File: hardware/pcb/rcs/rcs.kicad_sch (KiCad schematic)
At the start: 19 parts, among them J1 Conn_01x02_Socket, J2 Conn_01x02_Socket, J3 Conn_01x02_Socket, J4 Conn_01x02_Socket, J5 Conn_01x02_Socket, J6 Conn_01x02_Socket, Q1 BS170, Q2 BS170, Q3 BS170, Q4 BS170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

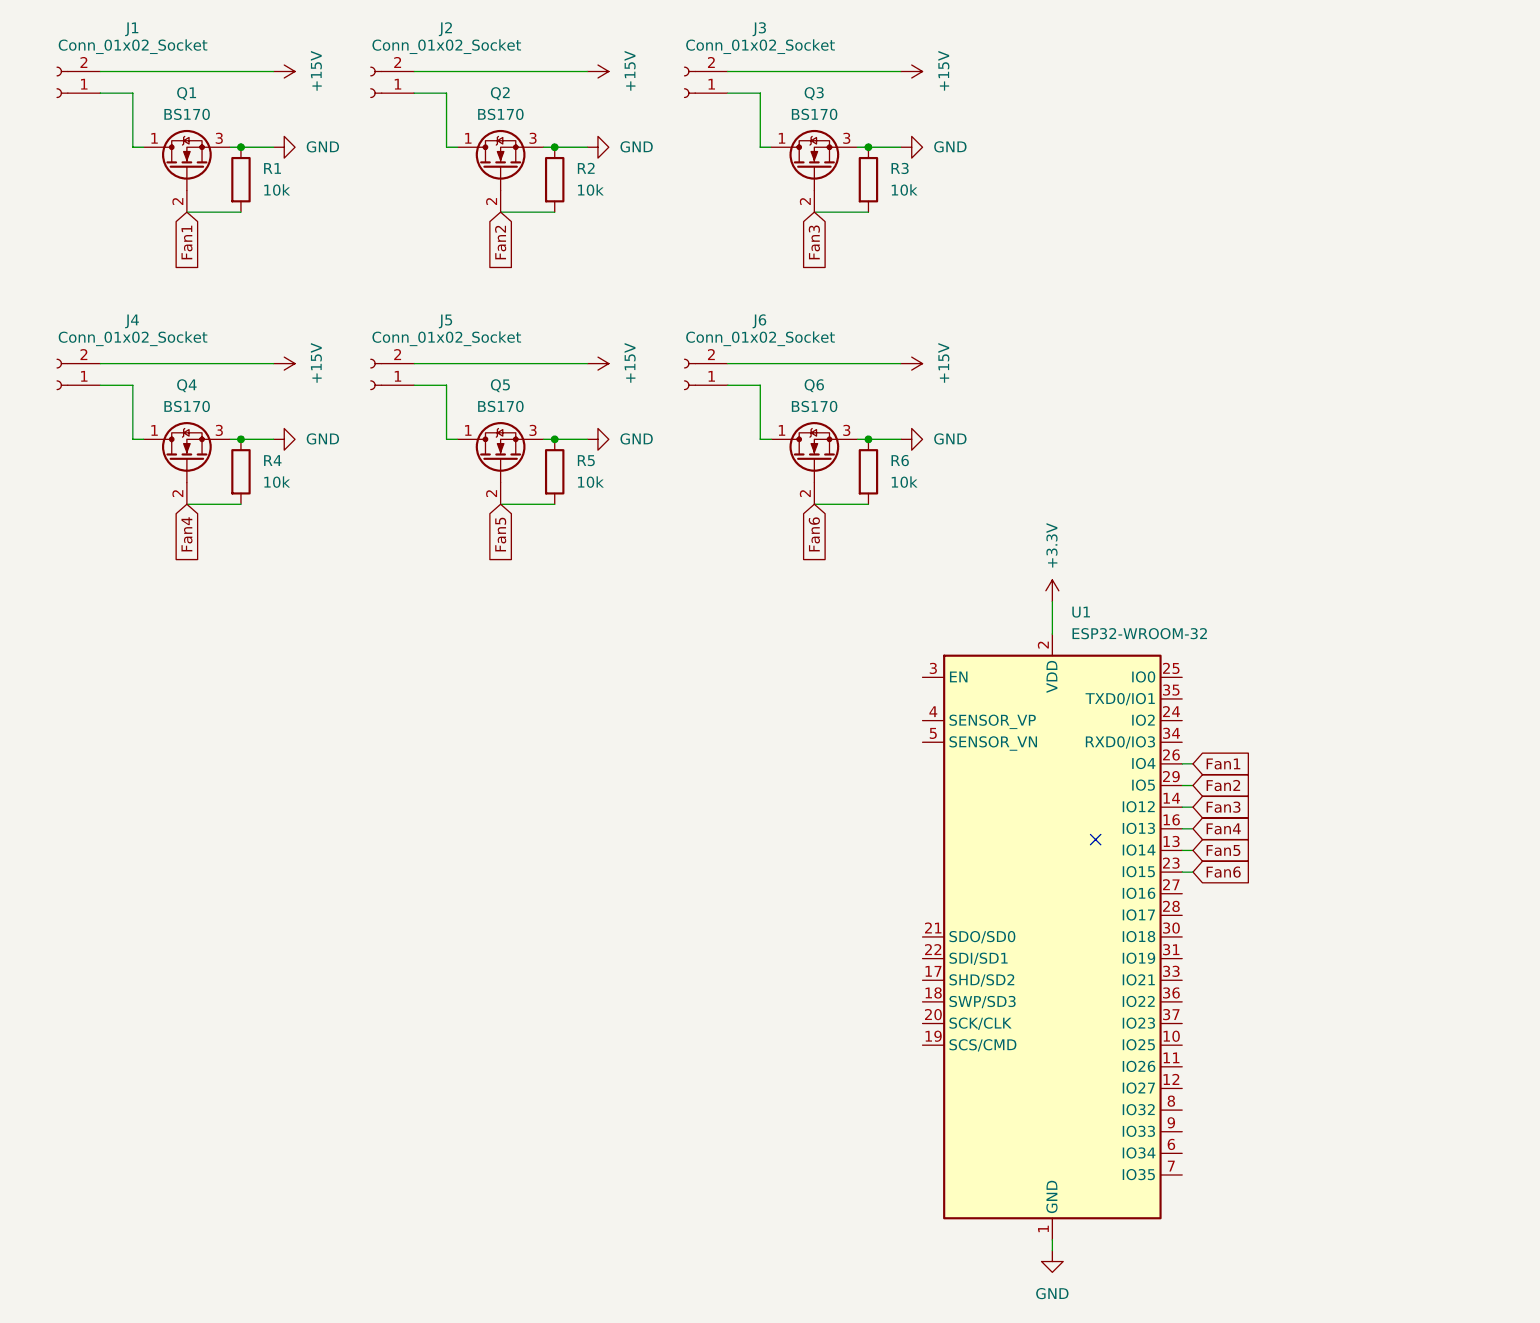
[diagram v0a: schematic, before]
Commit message: Add ESP32 dev board schematic and footprint, make draft PCB
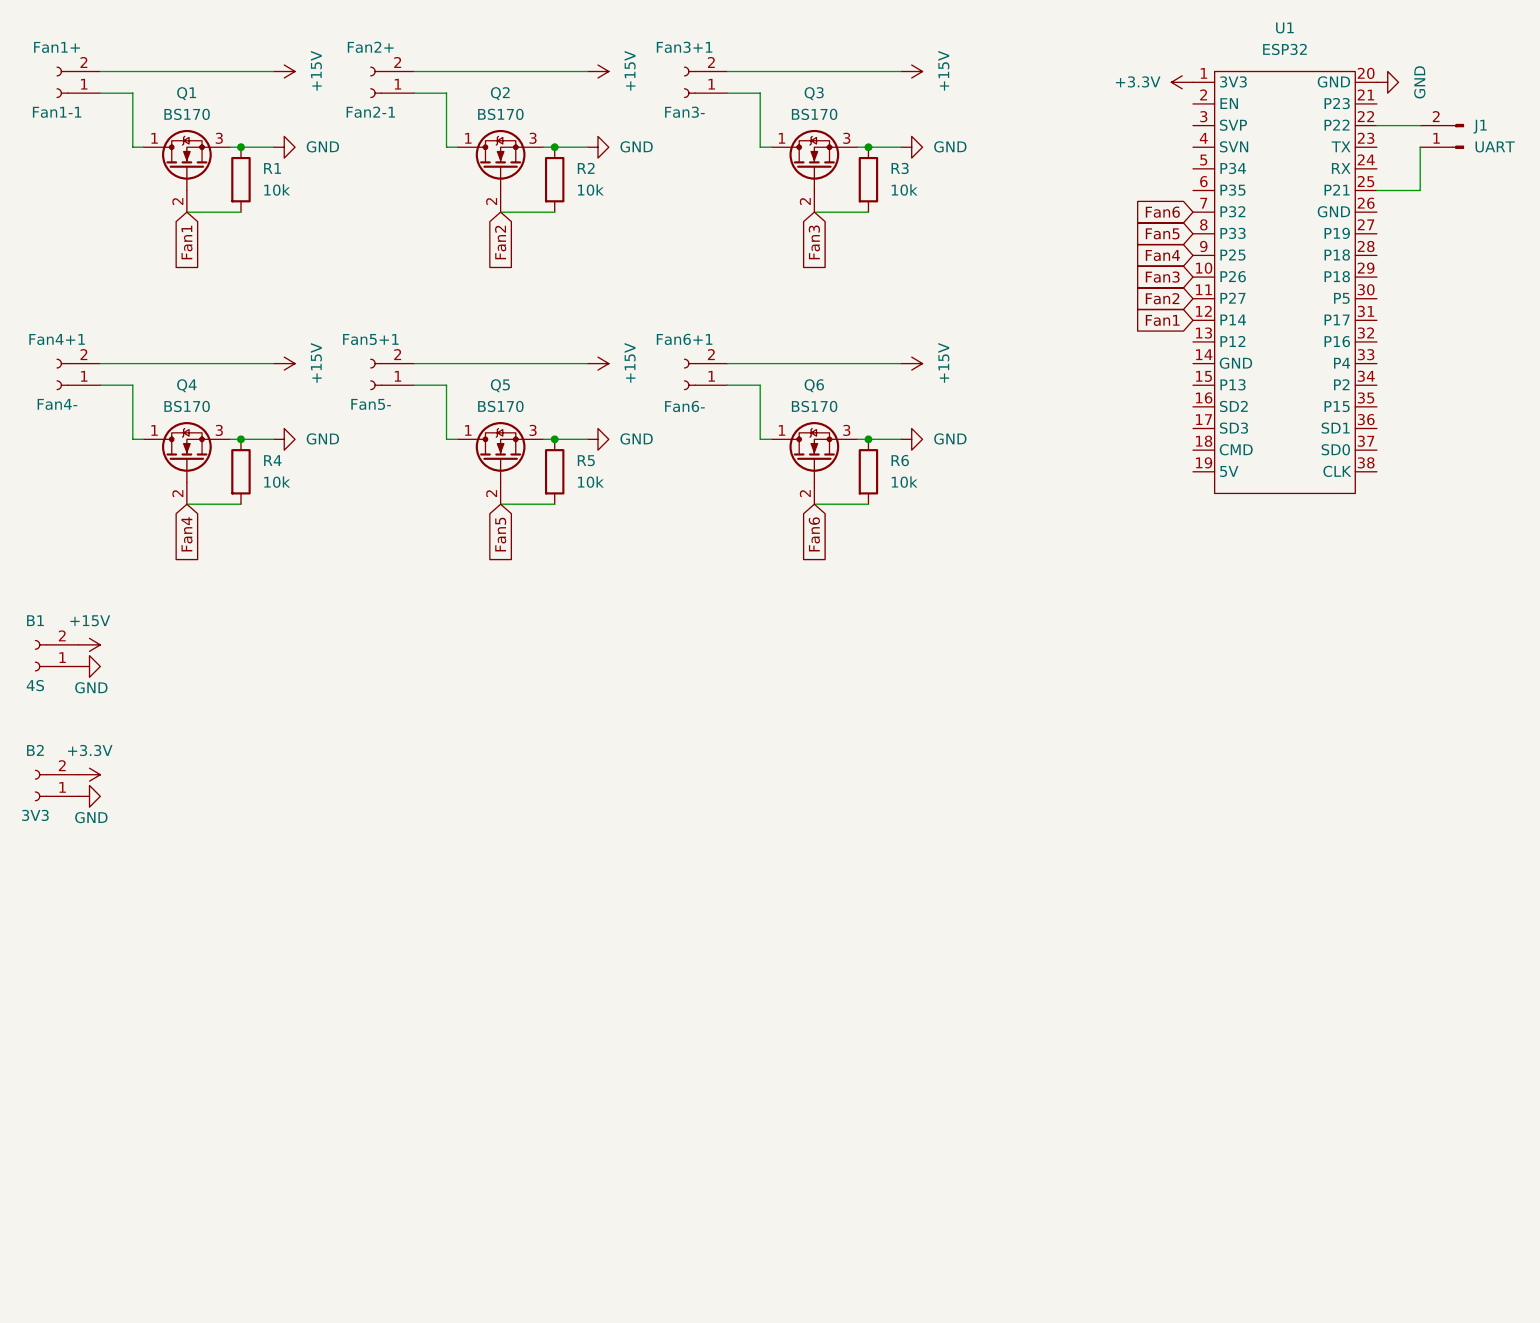
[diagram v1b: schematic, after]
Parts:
- removed U1: ESP32-WROOM-32, RF_Module:ESP32-WROOM-32, symbol RF_Module:ESP32-WROOM-32
- added B1: 4S, Connector_PinHeader_2.54mm:PinHeader_2x02_P2.54mm_Vertical, symbol Connector:Conn_01x02_Socket
- added B2: 3V3, Connector_PinHeader_2.54mm:PinHeader_2x02_P2.54mm_Vertical, symbol Connector:Conn_01x02_Socket
- added J1: UART, Connector_PinHeader_2.54mm:PinHeader_2x02_P2.54mm_Vertical, symbol Connector:Conn_01x02_Pin
- added U1: ESP32, custom:ESP32, symbol custom:ESP32
- Fan1-1: renamed from J1; value Conn_01x02_Socket -> Fan1+
- Fan2-1: renamed from J2; value Conn_01x02_Socket -> Fan2+
- Fan3+1: renamed from J3; value Conn_01x02_Socket -> Fan3-
- Fan4+1: renamed from J4; value Conn_01x02_Socket -> Fan4-
- Fan5+1: renamed from J5; value Conn_01x02_Socket -> Fan5-
- Fan6+1: renamed from J6; value Conn_01x02_Socket -> Fan6-
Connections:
- net +15V: now also B1.2 (Pin_2)
- net +3.3V: now also B2.2 (Pin_2), U1.1 (3V3)
- net Fan1: now also U1.12 (P14)
- net Fan2: now also U1.11 (P27)
- net Fan3: now also U1.10 (P26)
- net Fan4: now also U1.9 (P25)
- net Fan5: now also U1.8 (P33)
- net Fan6: now also U1.7 (P32)
- net GND: now also B1.1 (Pin_1), B2.1 (Pin_1), U1.20 (GND)
- new net: J1.1 (Pin_1), U1.25 (P21)
- new net: J1.2 (Pin_2), U1.22 (P22)
- no-connect marks 1 -> 0

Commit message: More compact PCB layout
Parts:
- B1, B2, J1: footprint Connector_PinHeader_2.54mm:PinHeader_2x02_P2.54mm_Vertical -> Connector_PinHeader_2.54mm:PinHeader_1x02_P2.54mm_Vertical
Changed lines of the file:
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@@
 			)
 		)
-		(property "Footprint" "Connector_PinHeader_2.54mm:PinHeader_2x02_P2.54mm_Vertical"
+		(property "Footprint" "Connector_PinHeader_2.54mm:PinHeader_1x02_P2.54mm_Vertical"
 			(at 191.77 34.29 0)
 			(effects
@@
 			)
 		)
-		(property "Footprint" "Connector_PinHeader_2.54mm:PinHeader_2x02_P2.54mm_Vertical"
+		(property "Footprint" "Connector_PinHeader_2.54mm:PinHeader_1x02_P2.54mm_Vertical"
 			(at 24.13 110.49 0)
 			(effects
@@
 			)
 		)
-		(property "Footprint" "Connector_PinHeader_2.54mm:PinHeader_2x02_P2.54mm_Vertical"
+		(property "Footprint" "Connector_PinHeader_2.54mm:PinHeader_1x02_P2.54mm_Vertical"
 			(at 24.13 95.25 0)
 			(effects

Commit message: Add minimum trace width and screw holes
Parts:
- Fan1-1, Fan2-1, Fan3+1, Fan4+1, Fan5+1, Fan6+1: footprint Connector_Wire:SolderWire-0.25sqmm_1x02_P4.2mm_D0.65mm_OD1.7mm -> Connector_PinHeader_2.54mm:PinHeader_1x02_P2.54mm_Vertical
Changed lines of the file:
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@@
 (kicad_sch
-	(version 20231120)
+	(version 20250114)
 	(generator "eeschema")
-	(generator_version "8.0")
+	(generator_version "9.0")
 	(paper "A4")
 	(junction
@@
 			)
 		)
-		(property "Footprint" "Connector_Wire:SolderWire-0.25sqmm_1x02_P4.2mm_D0.65mm_OD1.7mm"
+		(property "Footprint" "Connector_PinHeader_2.54mm:PinHeader_1x02_P2.54mm_Vertical"
 			(at 100.33 62.23 0)
 			(effects
@@
 			)
 		)
-		(property "Footprint" "Connector_Wire:SolderWire-0.25sqmm_1x02_P4.2mm_D0.65mm_OD1.7mm"
+		(property "Footprint" "Connector_PinHeader_2.54mm:PinHeader_1x02_P2.54mm_Vertical"
 			(at 100.33 27.94 0)
 			(effects
@@
 			)
 		)
-		(property "Footprint" "Connector_Wire:SolderWire-0.25sqmm_1x02_P4.2mm_D0.65mm_OD1.7mm"
+		(property "Footprint" "Connector_PinHeader_2.54mm:PinHeader_1x02_P2.54mm_Vertical"
 			(at 63.5 27.94 0)
 			(effects
@@
 			)
 		)
-		(property "Footprint" "Connector_Wire:SolderWire-0.25sqmm_1x02_P4.2mm_D0.65mm_OD1.7mm"
+		(property "Footprint" "Connector_PinHeader_2.54mm:PinHeader_1x02_P2.54mm_Vertical"
 			(at 63.5 62.23 0)
 			(effects
@@
 			)
 		)
-		(property "Footprint" "Connector_Wire:SolderWire-0.25sqmm_1x02_P4.2mm_D0.65mm_OD1.7mm"
+		(property "Footprint" "Connector_PinHeader_2.54mm:PinHeader_1x02_P2.54mm_Vertical"
 			(at 26.67 27.94 0)
 			(effects
@@
 			)
 		)
-		(property "Footprint" "Connector_Wire:SolderWire-0.25sqmm_1x02_P4.2mm_D0.65mm_OD1.7mm"
+		(property "Footprint" "Connector_PinHeader_2.54mm:PinHeader_1x02_P2.54mm_Vertical"
 			(at 26.67 62.23 0)
 			(effects
@@
 		)
 	)
+	(embedded_fonts no)
 )

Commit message: Increase trace width to 0.3mm
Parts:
- Q1, Q2, Q3, Q4, Q5, Q6: footprint Package_TO_SOT_THT:TO-92_Inline -> Package_TO_SOT_THT:TO-92_Inline_Wide
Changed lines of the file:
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@@
 			)
 		)
-		(property "Footprint" "Package_TO_SOT_THT:TO-92_Inline"
+		(property "Footprint" "Package_TO_SOT_THT:TO-92_Inline_Wide"
 			(at 80.645 31.75 0)
 			(effects
@@
 			)
 		)
-		(property "Footprint" "Package_TO_SOT_THT:TO-92_Inline"
+		(property "Footprint" "Package_TO_SOT_THT:TO-92_Inline_Wide"
 			(at 80.645 66.04 0)
 			(effects
@@
 			)
 		)
-		(property "Footprint" "Package_TO_SOT_THT:TO-92_Inline"
+		(property "Footprint" "Package_TO_SOT_THT:TO-92_Inline_Wide"
 			(at 43.815 31.75 0)
 			(effects
@@
 			)
 		)
-		(property "Footprint" "Package_TO_SOT_THT:TO-92_Inline"
+		(property "Footprint" "Package_TO_SOT_THT:TO-92_Inline_Wide"
 			(at 43.815 66.04 0)
 			(effects
@@
 			)
 		)
-		(property "Footprint" "Package_TO_SOT_THT:TO-92_Inline"
+		(property "Footprint" "Package_TO_SOT_THT:TO-92_Inline_Wide"
 			(at 117.475 31.75 0)
 			(effects
@@
 			)
 		)
-		(property "Footprint" "Package_TO_SOT_THT:TO-92_Inline"
+		(property "Footprint" "Package_TO_SOT_THT:TO-92_Inline_Wide"
 			(at 117.475 66.04 0)
 			(effects

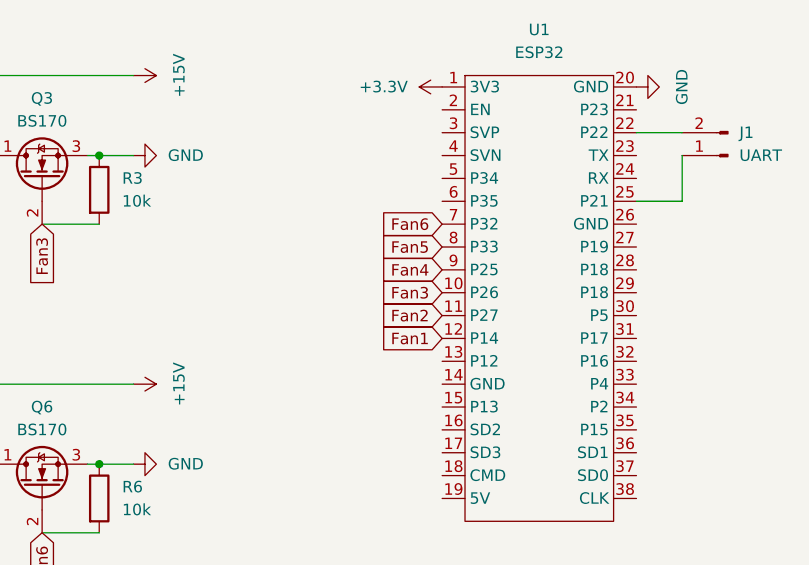
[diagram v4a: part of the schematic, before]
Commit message: Fix ESP32 USB port location
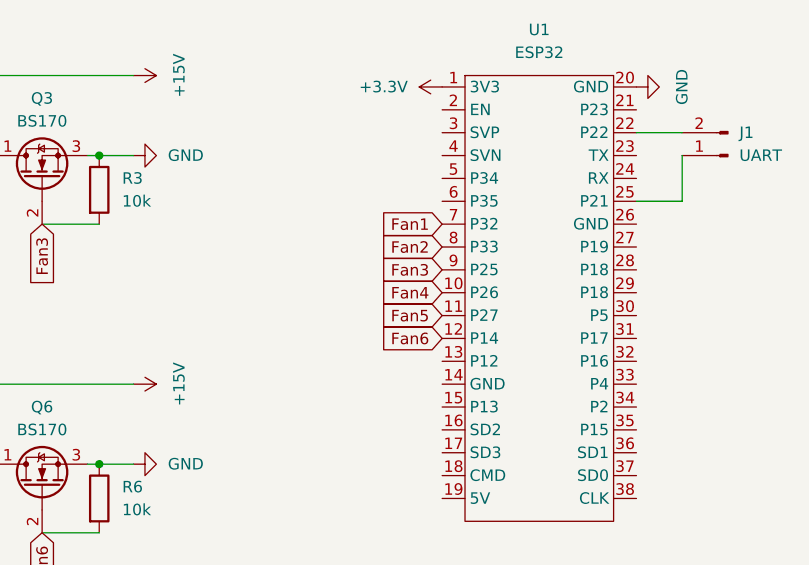
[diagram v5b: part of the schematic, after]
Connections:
- net Fan1: now also U1.7 (P32); no longer U1.12 (P14)
- net Fan2: now also U1.8 (P33); no longer U1.11 (P27)
- net Fan3: now also U1.9 (P25); no longer U1.10 (P26)
- net Fan4: now also U1.10 (P26); no longer U1.9 (P25)
- net Fan5: now also U1.11 (P27); no longer U1.8 (P33)
- net Fan6: now also U1.12 (P14); no longer U1.7 (P32)
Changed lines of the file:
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@@
 	(global_label "Fan5"
+		(shape input)
+		(at 160.02 52.07 180)
+		(fields_autoplaced yes)
+		(effects
+			(font
+				(size 1.27 1.27)
+			)
+			(justify right)
+		)
+		(property "Intersheetrefs" "${INTERSHEET_REFS}"
+			(at 152.4387 52.07 0)
+			(effects
+				(font
+					(size 1.27 1.27)
+				)
+				(justify right)
+				(hide yes)
+			)
+		)
+	)
+	(global_label "Fan2"
 		(shape input)
 		(at 160.02 44.45 180)
@@
 		)
 	)
-	(global_label "Fan2"
+	(global_label "Fan3"
 		(shape input)
-		(at 160.02 52.07 180)
+		(at 160.02 46.99 180)
 		(fields_autoplaced yes)
 		(effects
@@
 		)
 		(property "Intersheetrefs" "${INTERSHEET_REFS}"
-			(at 152.4387 52.07 0)
+			(at 152.4387 46.99 0)
 			(effects
 				(font
@@
 		)
 	)
-	(global_label "Fan3"
+	(global_label "Fan4"
 		(shape input)
 		(at 160.02 49.53 180)
@@
 		)
 	)
-	(global_label "Fan4"
+	(global_label "Fan6"
 		(shape input)
-		(at 160.02 46.99 180)
+		(at 160.02 54.61 180)
 		(fields_autoplaced yes)
 		(effects
@@
 		)
 		(property "Intersheetrefs" "${INTERSHEET_REFS}"
-			(at 152.4387 46.99 0)
+			(at 152.4387 54.61 0)
 			(effects
 				(font
@@
 		)
 	)
-	(global_label "Fan6"
+	(global_label "Fan1"
 		(shape input)
 		(at 160.02 41.91 180)
@@
 			(effects
 				(font
-					(size 1.27 1.27)
-				)
-				(justify right)
-				(hide yes)
-			)
-		)
-	)
-	(global_label "Fan1"
-		(shape input)
-		(at 160.02 54.61 180)
-		(fields_autoplaced yes)
-		(effects
-			(font
-				(size 1.27 1.27)
-			)
-			(justify right)
-		)
-		(property "Intersheetrefs" "${INTERSHEET_REFS}"
-			(at 152.4387 54.61 0)
-			(effects
-				(font

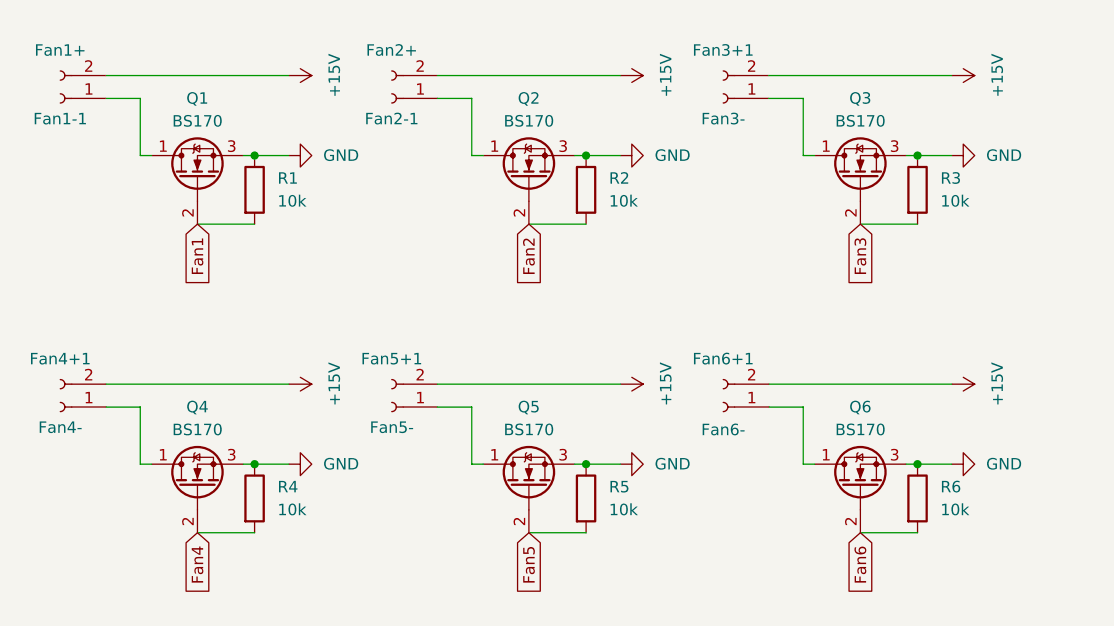
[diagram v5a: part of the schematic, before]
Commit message: Add flyback diodes
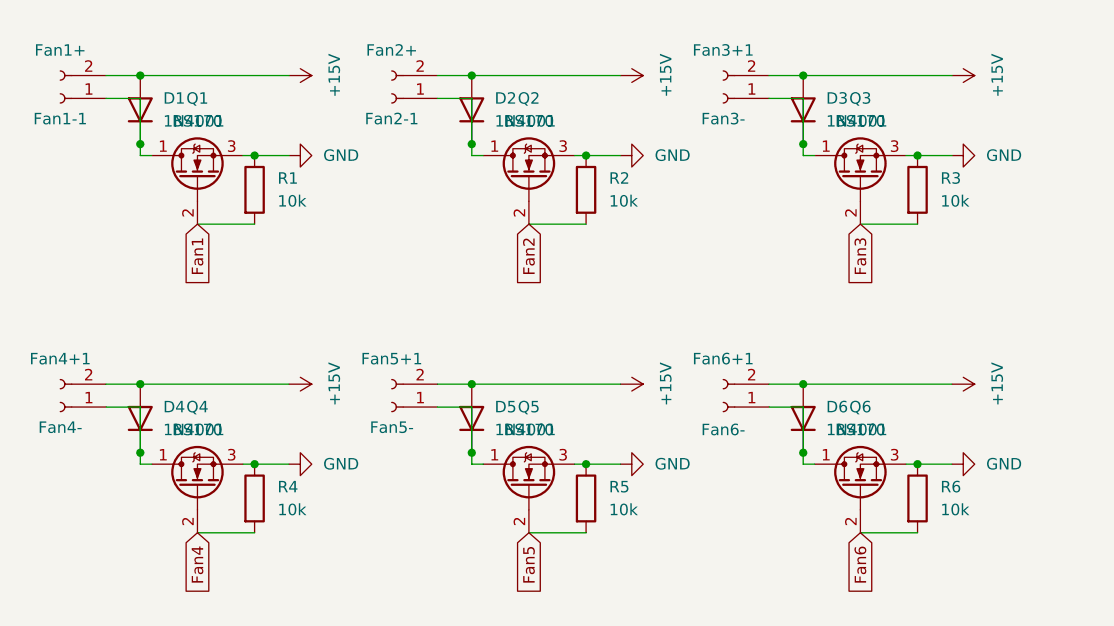
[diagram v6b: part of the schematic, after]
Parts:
- added D1, D2, D3, D4, D5, D6: 1N4001, Diode_THT:D_DO-41_SOD81_P7.62mm_Horizontal, symbol Diode:1N4001
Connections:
- net +15V: now also D1.2 (A), D2.2 (A), D3.2 (A), D4.2 (A), D5.2 (A), D6.2 (A)
- net at Fan6+1.1 (Pin_1), Q6.1 (D): now also D6.1 (K)
- net at Fan2-1.1 (Pin_1), Q2.1 (D): now also D2.1 (K)
- net at Fan5+1.1 (Pin_1), Q5.1 (D): now also D5.1 (K)
- net at Fan3+1.1 (Pin_1), Q3.1 (D): now also D3.1 (K)
- net at Fan1-1.1 (Pin_1), Q1.1 (D): now also D1.1 (K)
- net at Fan4+1.1 (Pin_1), Q4.1 (D): now also D4.1 (K)
